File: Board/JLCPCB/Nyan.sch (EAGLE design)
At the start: 64 parts, among them IC1 74HCT541PW, IC2 STM32F10XCXT6, IC3 74HCT541PW, IC4 ST3485, U2 A4988_STEP, U3 MAX6966, X1 WR-WTB2.0-2_THT-VER, X10 32768, X2 WR-WTB2.0-4_THT_VER, X3 WR-WTB2.0-5_THT-VER, X4 WR-WTB2.0-5_THT-VER, X6 68610614122, X7 68612414422, X8 68610414122, X9 8M

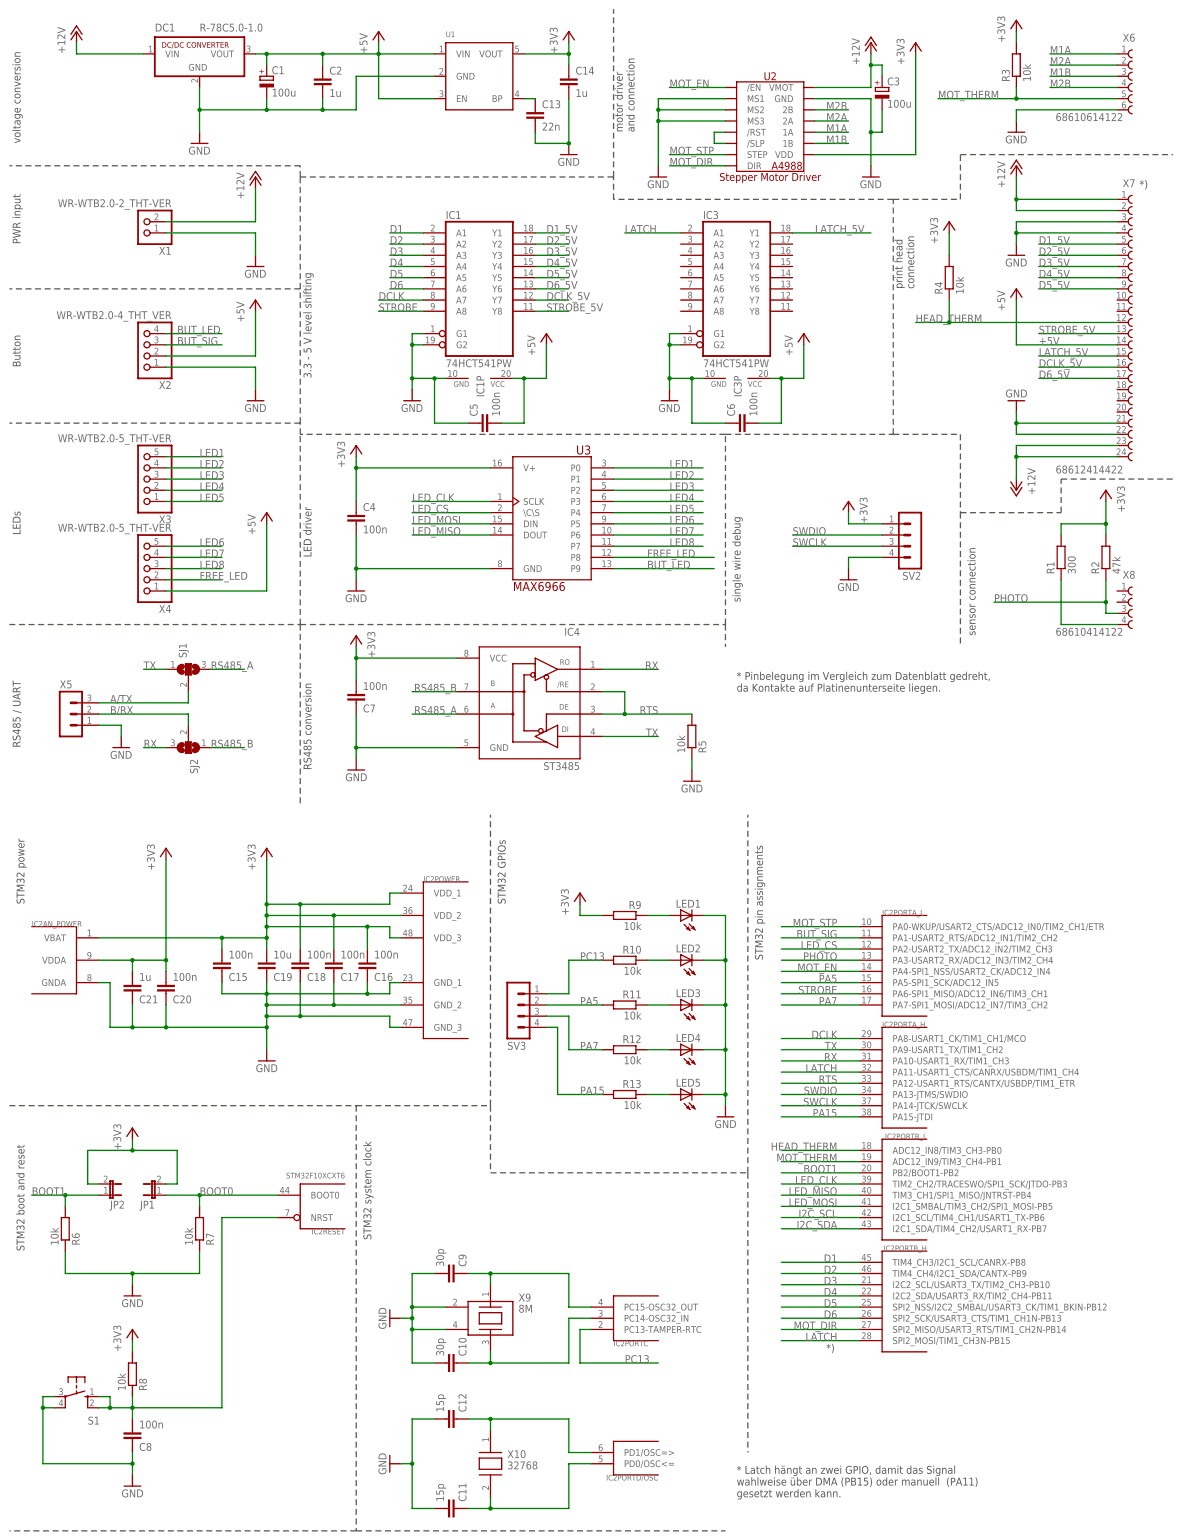
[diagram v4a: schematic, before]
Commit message: [Board] Silk Screen Top done
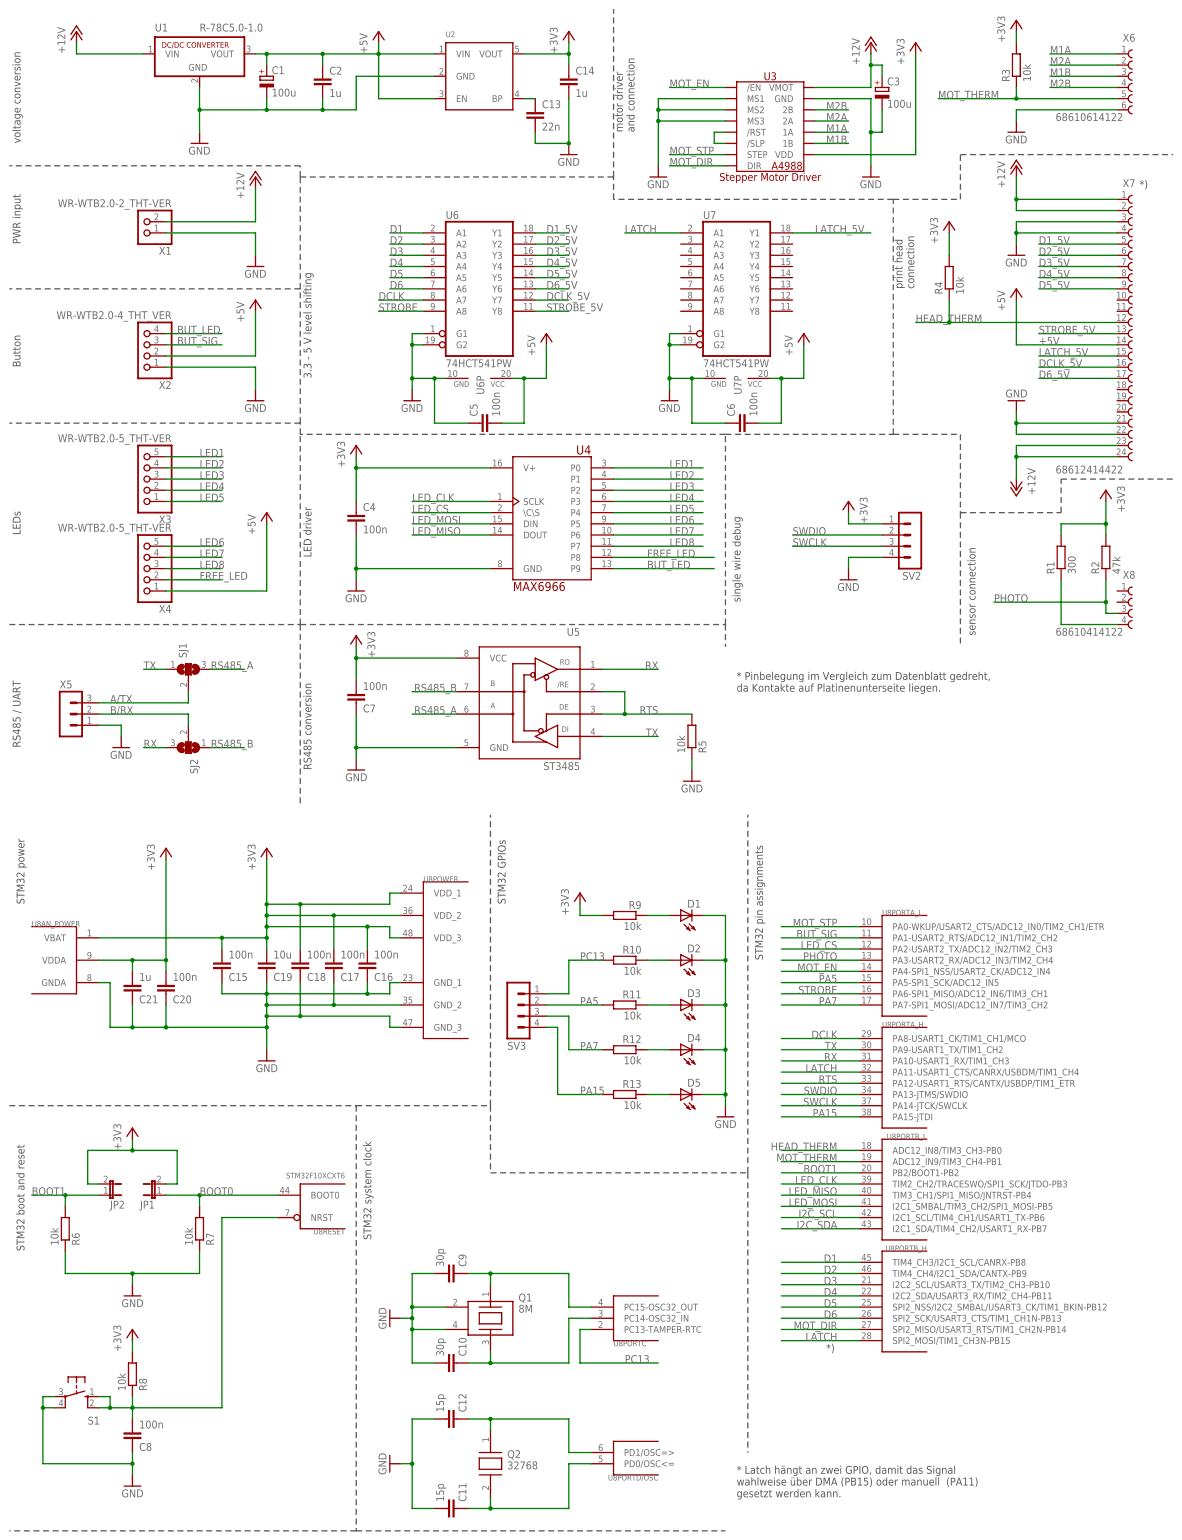
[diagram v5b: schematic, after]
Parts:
- removed DC1: R-78C5.0-1.0, dc-dc-converter:R-78C5.0-1.0
- added U4: MAX6966, meineLibrary:MAX6966
- U1: value (none) -> R-78C5.0-1.0; device Power:RT9193 -> dc-dc-converter:R-78C5.0-1.0
- U2: value A4988_STEP -> (none); device robotics:A4988_STEP -> Power:RT9193
- U3: value MAX6966 -> A4988_STEP; device meineLibrary:MAX6966 -> robotics:A4988_STEP
- renumbered IC1 to U6, IC2 to U8, IC3 to U7, IC4 to U5, LED1 to D1, LED2 to D2, LED3 to D3, LED4 to D4, LED5 to D5, X10 to Q2, X9 to Q1
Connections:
- net +12V: now also U1.VIN, U3.VMOT; no longer DC1.VIN, U2.VMOT
- net +3V3: now also U2.VOUT, U3.VDD, U4.V+; no longer U1.VOUT, U2.VDD, U3.V+
- net +5V: now also U1.VOUT, U2.EN, U2.VIN; no longer DC1.VOUT, U1.EN, U1.VIN
- net BUT_LED: now also U4.P9; no longer U3.P9
- net FREE_LED: now also U4.P8; no longer U3.P8
- net GND: now also U3.MS1, U3.MS2, U3.MS3, U4.GND; no longer DC1.GND, U2.MS1, U2.MS2, U2.MS3
- net LED1: now also U4.P0; no longer U3.P0
- net LED2: now also U4.P1; no longer U3.P1
- net LED3: now also U4.P2; no longer U3.P2
- net LED4: now also U4.P3; no longer U3.P3
- net LED5: now also U4.P4; no longer U3.P4
- net LED6: now also U4.P5; no longer U3.P5
- net LED7: now also U4.P6; no longer U3.P6
- net LED8: now also U4.P7; no longer U3.P7
- net LED_CLK: now also U4.SCLK; no longer U3.SCLK
- net LED_CS: now also U4.\C\S; no longer U3.\C\S
- net LED_MISO: now also U4.DOUT; no longer U3.DOUT
- net LED_MOSI: now also U4.DIN; no longer U3.DIN
- net M1A: now also U3.1A; no longer U2.1A
- net M1B: now also U3.1B; no longer U2.1B
- net M2A: now also U3.2A; no longer U2.2A
- net M2B: now also U3.2B; no longer U2.2B
- net MOT_DIR: now also U3.DIR; no longer U2.DIR
- net MOT_EN: now also U3./EN; no longer U2./EN
- net MOT_STP: now also U3.STEP; no longer U2.STEP
- net N$19: now also U2.BP; no longer U1.BP
- net N$2: now also U3./RST, U3./SLP; no longer U2./RST, U2./SLP

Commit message: [Board] Silkscreen done, DRC checked
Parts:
- U3: device robotics:A4988_STEP -> IC:A4988_STEP
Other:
- note added: "* Latch is attached to two GPIOs, so that the signal can either be set by DMA (PB15) or manually (PA11)."
- note removed: "* Latch hängt an zwei GPIO, damit das Signal wahlweise über DMA (PB15) oder manuell (PA11) gesetzt werden kann."
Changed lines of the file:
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@@
 <part name="X6" library="Wuerth_Elektronik_eiCan_03_ZIF_Connectors_Flat_Flexible_Cable" deviceset="68610614122" device=""/>
 <part name="X7" library="Wuerth_Elektronik_eiCan_03_ZIF_Connectors_Flat_Flexible_Cable" deviceset="68612414422" device=""/>
-<part name="U3" library="robotics" deviceset="A4988_STEP" device=""/>
+<part name="U3" library="IC" deviceset="A4988_STEP" device=""/>
 <part name="U4" library="meineLibrary" deviceset="MAX6966" device=""/>
 <part name="P+1" library="supply1" deviceset="+5V" device=""/>
@@
 <text x="2.54" y="60.96" size="1.778" layer="97" rot="R90">LEDs</text>
 <text x="2.54" y="12.7" size="1.778" layer="97" rot="R90">RS485 / UART</text>
-<text x="165.1" y="-157.48" size="1.778" layer="97">* Latch hängt an zwei GPIO, damit das Signal
-wahlweise über DMA (PB15) oder manuell  (PA11)
-gesetzt werden kann.</text>
+<text x="165.1" y="-157.48" size="1.778" layer="97">* Latch is attached to two GPIOs,
+so that the signal can either be set
+by DMA (PB15) or manually  (PA11).</text>
 <text x="165.1" y="25.4" size="1.778" layer="97">* Pinbelegung im Vergleich zum Datenblatt gedreht,
 da Kontakte auf Platinenunterseite liegen.</text>

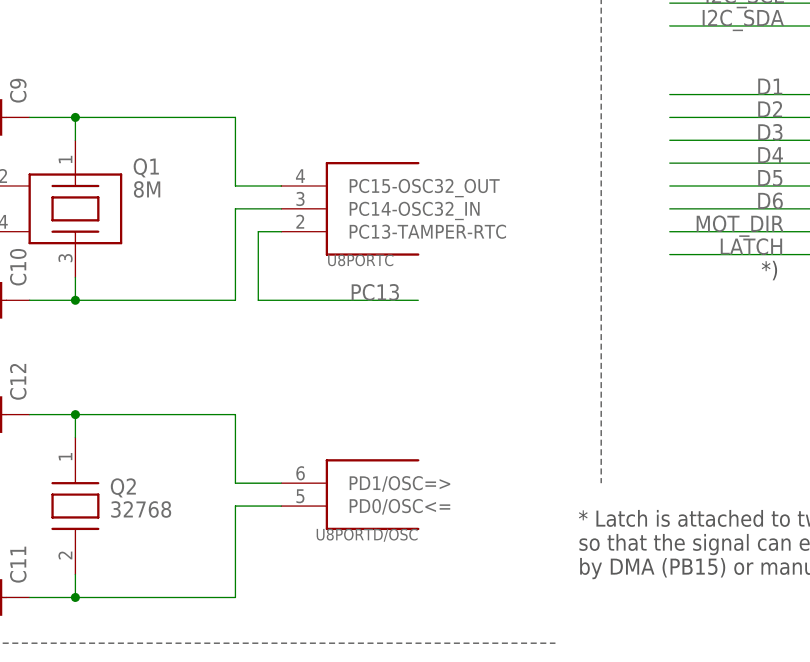
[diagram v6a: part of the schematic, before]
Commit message: [Board] Fixed connection for crystals
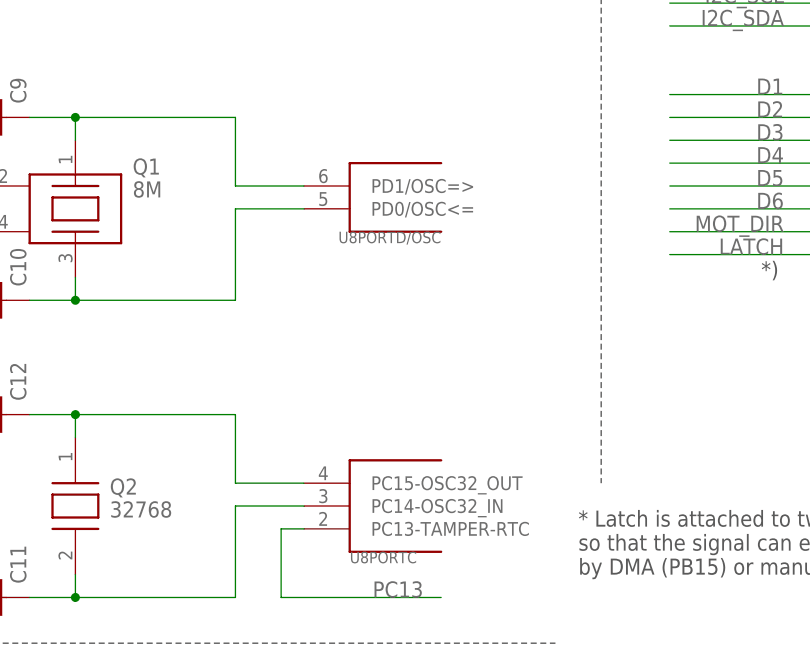
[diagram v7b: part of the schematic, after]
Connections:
- net N$10: now also U8PORTC.PC14-OSC32_IN; no longer U8PORTD/OSC.PD0/OSC<=
- net N$11: now also U8PORTD/OSC.PD0/OSC<=; no longer U8PORTC.PC14-OSC32_IN
- net N$14: now also U8PORTD/OSC.PD1/OSC=>; no longer U8PORTC.PC15-OSC32_OUT
- net N$9: now also U8PORTC.PC15-OSC32_OUT; no longer U8PORTD/OSC.PD1/OSC=>
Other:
- moved on the sheet: U8PORTC, U8PORTD/OSC
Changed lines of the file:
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@@
 <instance part="U8" gate="PORTB_H" x="203.2" y="-111.76" rot="MR0"/>
 <instance part="U8" gate="POWER" x="99.06" y="-35.56"/>
-<instance part="U8" gate="PORTC" x="139.7" y="-116.84" rot="MR180"/>
-<instance part="U8" gate="PORTD/OSC" x="139.7" y="-149.86" rot="R180"/>
+<instance part="U8" gate="PORTC" x="142.24" y="-149.86" rot="MR180"/>
+<instance part="U8" gate="PORTD/OSC" x="142.24" y="-116.84" rot="R180"/>
 <instance part="U8" gate="AN_POWER" x="10.16" y="-35.56"/>
 <instance part="U8" gate="RESET" x="71.12" y="-91.44" rot="R180"/>
@@
 <wire x1="109.22" y1="-142.24" x2="109.22" y2="-139.7" width="0.1524" layer="91"/>
 <wire x1="109.22" y1="-139.7" x2="127" y2="-139.7" width="0.1524" layer="91"/>
-<pinref part="U8" gate="PORTD/OSC" pin="PD1/OSC=&gt;"/>
 <wire x1="127" y1="-139.7" x2="127" y2="-147.32" width="0.1524" layer="91"/>
-<wire x1="127" y1="-147.32" x2="132.08" y2="-147.32" width="0.1524" layer="91"/>
 <pinref part="C12" gate="G$1" pin="1"/>
 <wire x1="104.14" y1="-139.7" x2="109.22" y2="-139.7" width="0.1524" layer="91"/>
 <junction x="109.22" y="-139.7"/>
+<pinref part="U8" gate="PORTC" pin="PC15-OSC32_OUT"/>
+<wire x1="127" y1="-147.32" x2="134.62" y2="-147.32" width="0.1524" layer="91"/>
 </segment>
 </net>
@@
 <wire x1="109.22" y1="-157.48" x2="109.22" y2="-160.02" width="0.1524" layer="91"/>
 <wire x1="109.22" y1="-160.02" x2="127" y2="-160.02" width="0.1524" layer="91"/>
-<pinref part="U8" gate="PORTD/OSC" pin="PD0/OSC&lt;="/>
 <wire x1="127" y1="-160.02" x2="127" y2="-149.86" width="0.1524" layer="91"/>
-<wire x1="127" y1="-149.86" x2="132.08" y2="-149.86" width="0.1524" layer="91"/>
 <pinref part="C11" gate="G$1" pin="1"/>
 <wire x1="104.14" y1="-160.02" x2="109.22" y2="-160.02" width="0.1524" layer="91"/>
 <junction x="109.22" y="-160.02"/>
+<pinref part="U8" gate="PORTC" pin="PC14-OSC32_IN"/>
+<wire x1="134.62" y1="-149.86" x2="127" y2="-149.86" width="0.1524" layer="91"/>
 </segment>
 </net>
@@
 <wire x1="109.22" y1="-127" x2="127" y2="-127" width="0.1524" layer="91"/>
 <wire x1="127" y1="-127" x2="127" y2="-116.84" width="0.1524" layer="91"/>
-<pinref part="U8" gate="PORTC" pin="PC14-OSC32_IN"/>
-<wire x1="127" y1="-116.84" x2="132.08" y2="-116.84" width="0.1524" layer="91"/>
 <pinref part="C10" gate="G$1" pin="1"/>
 <wire x1="104.14" y1="-127" x2="109.22" y2="-127" width="0.1524" layer="91"/>
 <junction x="109.22" y="-127"/>
+<pinref part="U8" gate="PORTD/OSC" pin="PD0/OSC&lt;="/>
+<wire x1="127" y1="-116.84" x2="134.62" y2="-116.84" width="0.1524" layer="91"/>
 </segment>
 </net>
@@
 <wire x1="109.22" y1="-106.68" x2="127" y2="-106.68" width="0.1524" layer="91"/>
 <wire x1="127" y1="-106.68" x2="127" y2="-114.3" width="0.1524" layer="91"/>
-<pinref part="U8" gate="PORTC" pin="PC15-OSC32_OUT"/>
-<wire x1="127" y1="-114.3" x2="132.08" y2="-114.3" width="0.1524" layer="91"/>
 <pinref part="C9" gate="G$1" pin="1"/>
 <wire x1="104.14" y1="-106.68" x2="109.22" y2="-106.68" width="0.1524" layer="91"/>
 <junction x="109.22" y="-106.68"/>
+<pinref part="U8" gate="PORTD/OSC" pin="PD1/OSC=&gt;"/>
+<wire x1="127" y1="-114.3" x2="134.62" y2="-114.3" width="0.1524" layer="91"/>
 </segment>
 </net>
@@
 <segment>
 <pinref part="U8" gate="PORTC" pin="PC13-TAMPER-RTC"/>
-<wire x1="132.08" y1="-119.38" x2="129.54" y2="-119.38" width="0.1524" layer="91"/>
-<wire x1="129.54" y1="-119.38" x2="129.54" y2="-127" width="0.1524" layer="91"/>
-<wire x1="129.54" y1="-127" x2="147.32" y2="-127" width="0.1524" layer="91"/>
-<label x="139.7" y="-127" size="1.778" layer="95"/>
-</segment>
-</net>
+<wire x1="134.62" y1="-152.4" x2="132.08" y2="-152.4" width="0.1524" layer="91"/>
+<wire x1="132.08" y1="-152.4" x2="132.08" y2="-160.02" width="0.1524" layer="91"/>
+<wire x1="132.08" y1="-160.02" x2="149.86" y2="-160.02" width="0.1524" layer="91"/>
+<label x="142.24" y="-160.02" size="1.778" layer="95"/>
+</segment>
+</net>
